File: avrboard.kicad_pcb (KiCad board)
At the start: 2 copper layers, 21 parts, among them IC1 ATMEGA328P-P, P1 FTDI, P2 ICSP, SW1 RESET, X1 16MHz

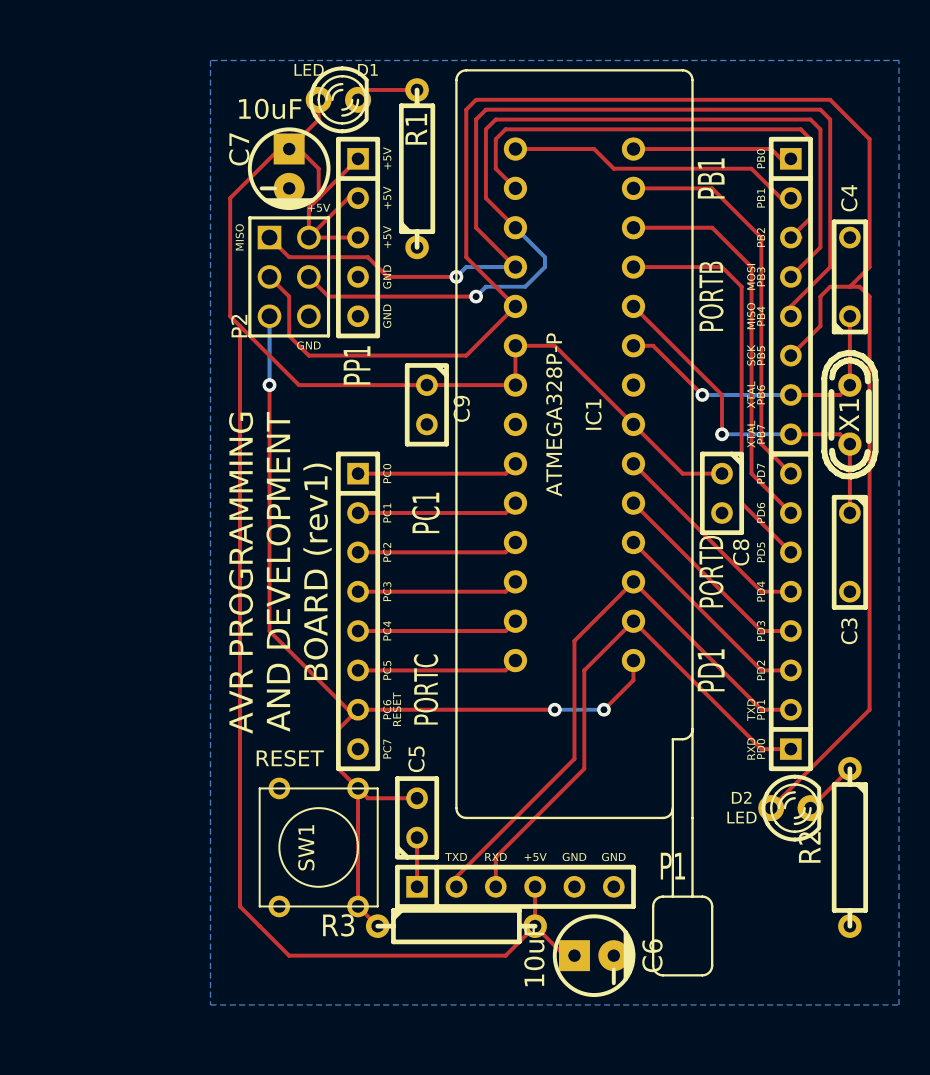
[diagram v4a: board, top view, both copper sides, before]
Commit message: Move the PORTB headers to the other side of the chip.
The routing is less crazy this way, since many of the port B pins are on
that side, and the power and port B headers can both fit together on that
side.
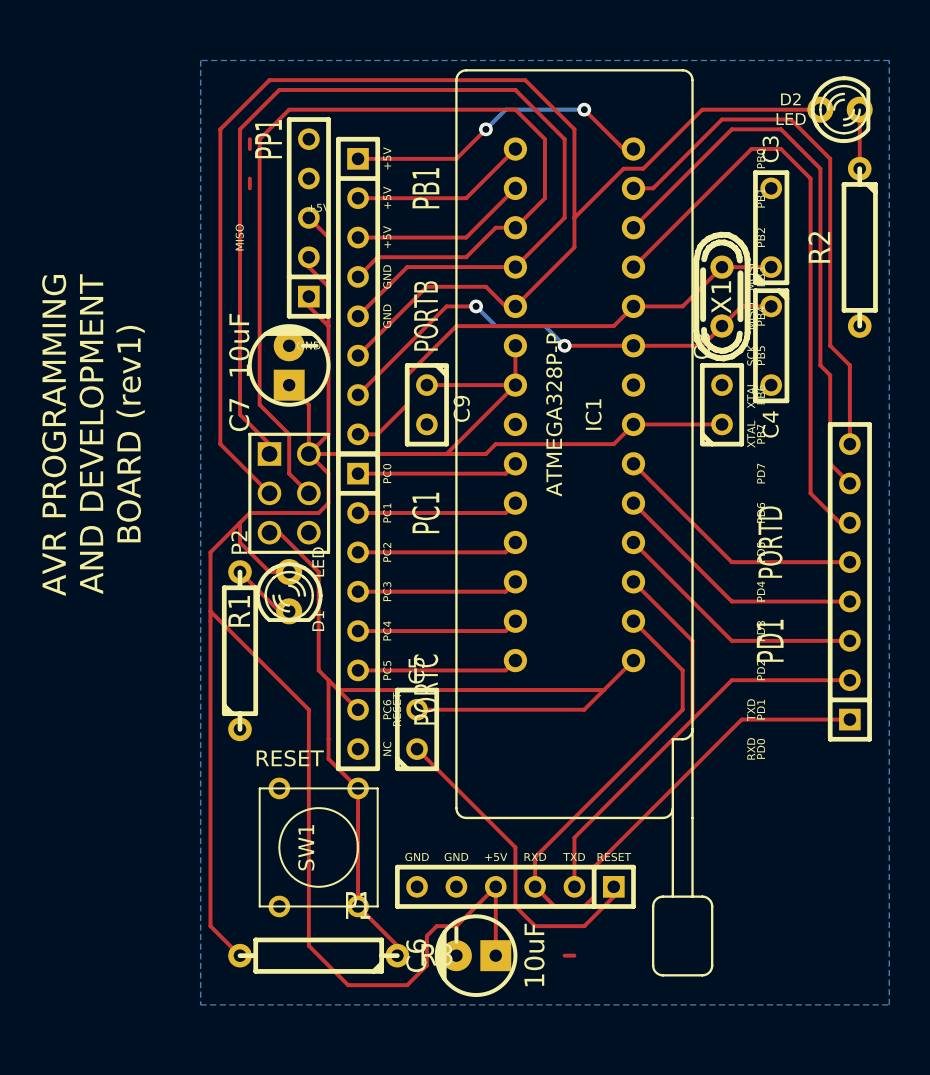
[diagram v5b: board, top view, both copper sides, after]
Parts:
- moved D2 45.2 mm to (164.5, 38.7)
- moved R2 38.7 mm to (165.7, 47.6)
- moved R1 33.1 mm to (125.7, 73.7)
- moved D1 31.9 mm to (128.9, 69.8), turned to 270 degrees
- moved PB1 27.9 mm to (133.3, 50.8)
- moved C3 21.6 mm to (160.0, 46.4), turned to 90 degrees
- moved P2 14.0 mm to (128.9, 63.5)
- moved C7 12.7 mm to (128.9, 55.2), turned to 0 degrees
- moved X1 11.2 mm to (156.8, 50.8), turned to 270 degrees
- moved R3 9.09 mm to (130.8, 93.3), turned to 180 degrees
- moved C6 7.62 mm to (141.0, 93.3), turned to 90 degrees
- moved C4 6.75 mm to (160.0, 54.0), turned to 270 degrees
- moved C5 5.72 mm to (137.2, 78.7)
- moved C8 5.72 mm to (156.8, 57.8), turned to 90 degrees
- moved PP1 4.96 mm to (130.2, 44.5), turned to 90 degrees
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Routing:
- net /PB5: track 116.1 -> 94.6 mm
- net /PB2: track 32.1 -> 11.5 mm
- net /+5V: track 139.5 -> 159.0 mm
- net Net-(C5-Pad1): track 3.18 -> 21.1 mm
- net /RXD: track 34.4 -> 49.4 mm
- net /PD5: track 26.0 -> 39.0 mm
- net /PD6: track 25.6 -> 36.9 mm
- net /PB6: track 20.0 -> 31.1 mm, vias 1 -> 2
- net /PB0: track 10.4 -> 20.1 mm, vias 0 -> 2
- net /PD7: track 25.6 -> 34.5 mm
- net /PB7: track 23.6 -> 32.3 mm, vias 1 -> 0
- net /PB1: track 19.1 -> 11.5 mm
- net /PD4: track 13.6 -> 16.6 mm
- net /PD3: track 13.6 -> 16.6 mm
- net /PD2: track 13.6 -> 16.6 mm
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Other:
- board text added: "NC"
- board text removed: "PC7"

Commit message: Clean up the silkscreen and remove some "bays" from the ground plane.
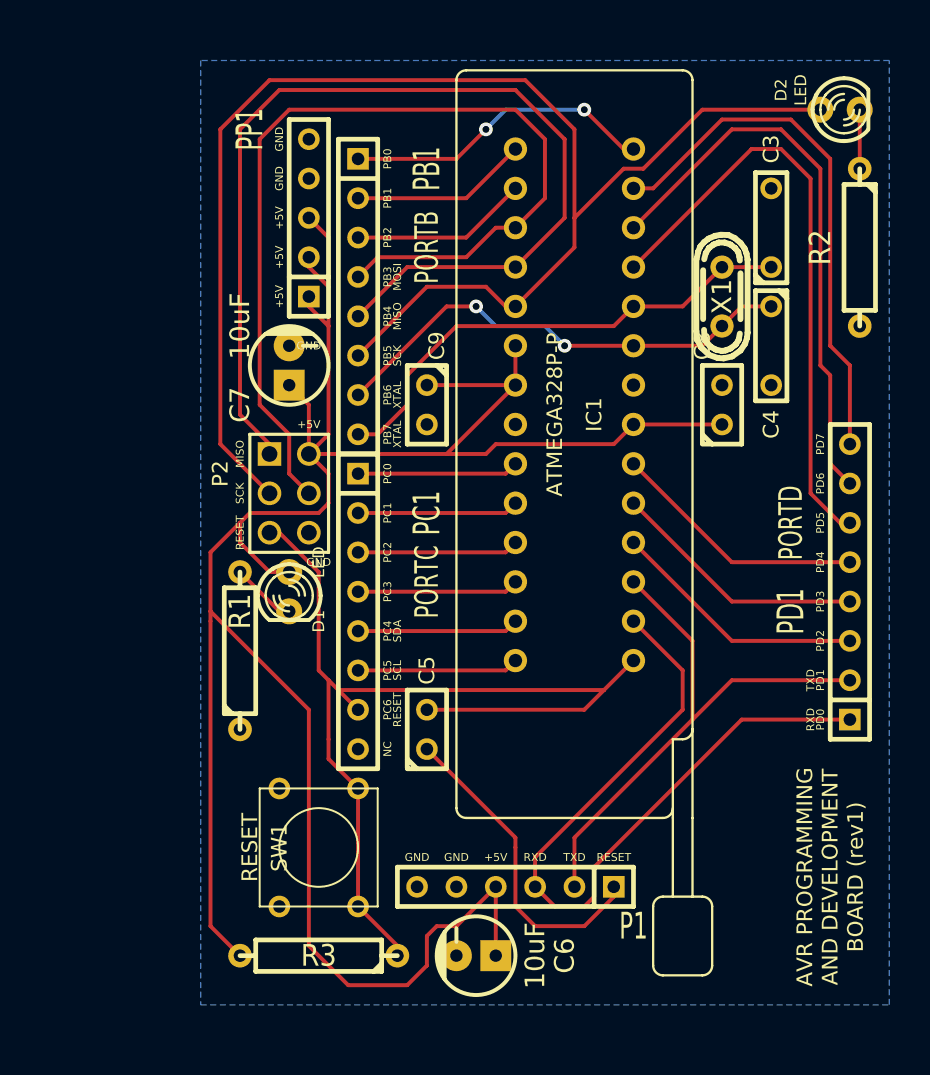
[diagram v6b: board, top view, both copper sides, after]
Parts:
- moved C5 0.63 mm to (137.8, 78.7)
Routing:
- net (no net): track 1.90 -> 0.00 mm
- net /RESET: track 66.2 -> 65.6 mm
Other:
- board text added: "SCL"
- board text added: "SDA"

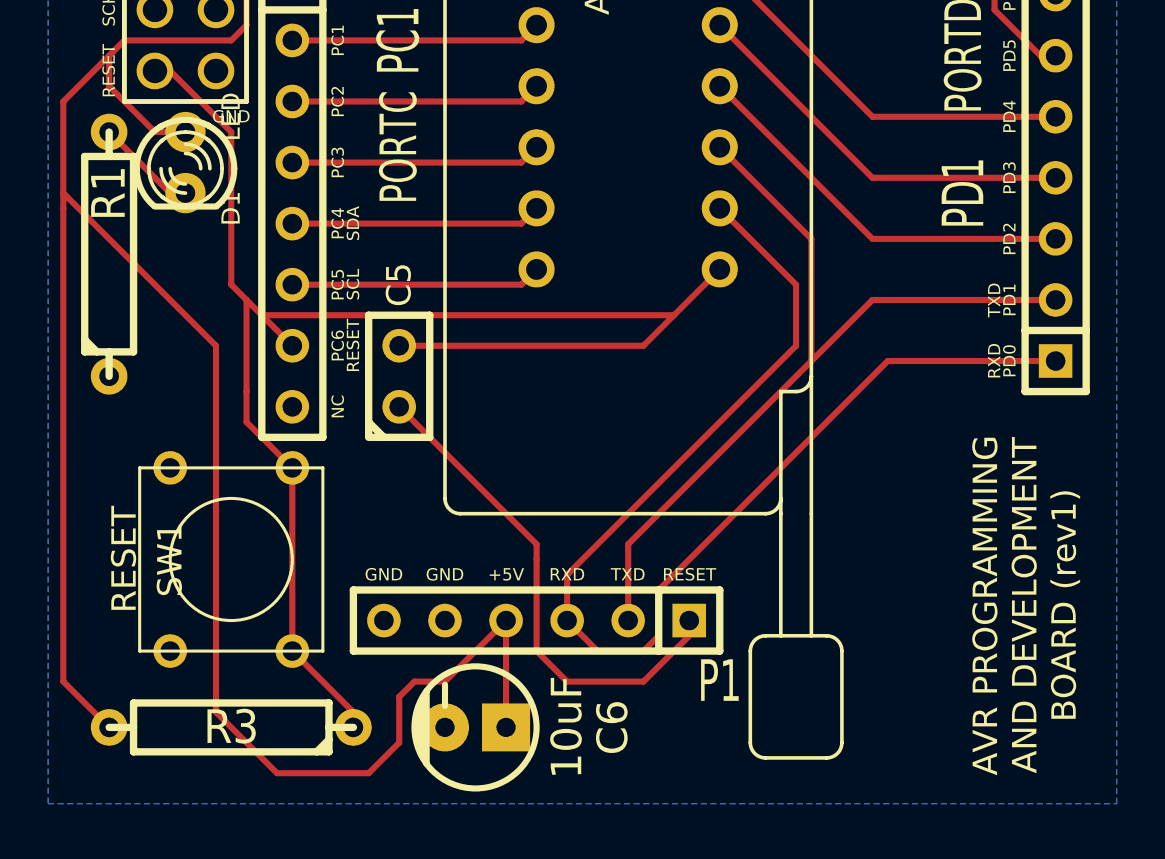
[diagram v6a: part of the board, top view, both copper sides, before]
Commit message: Move the FTDI socket over to increase clearance from the ZIF lever.
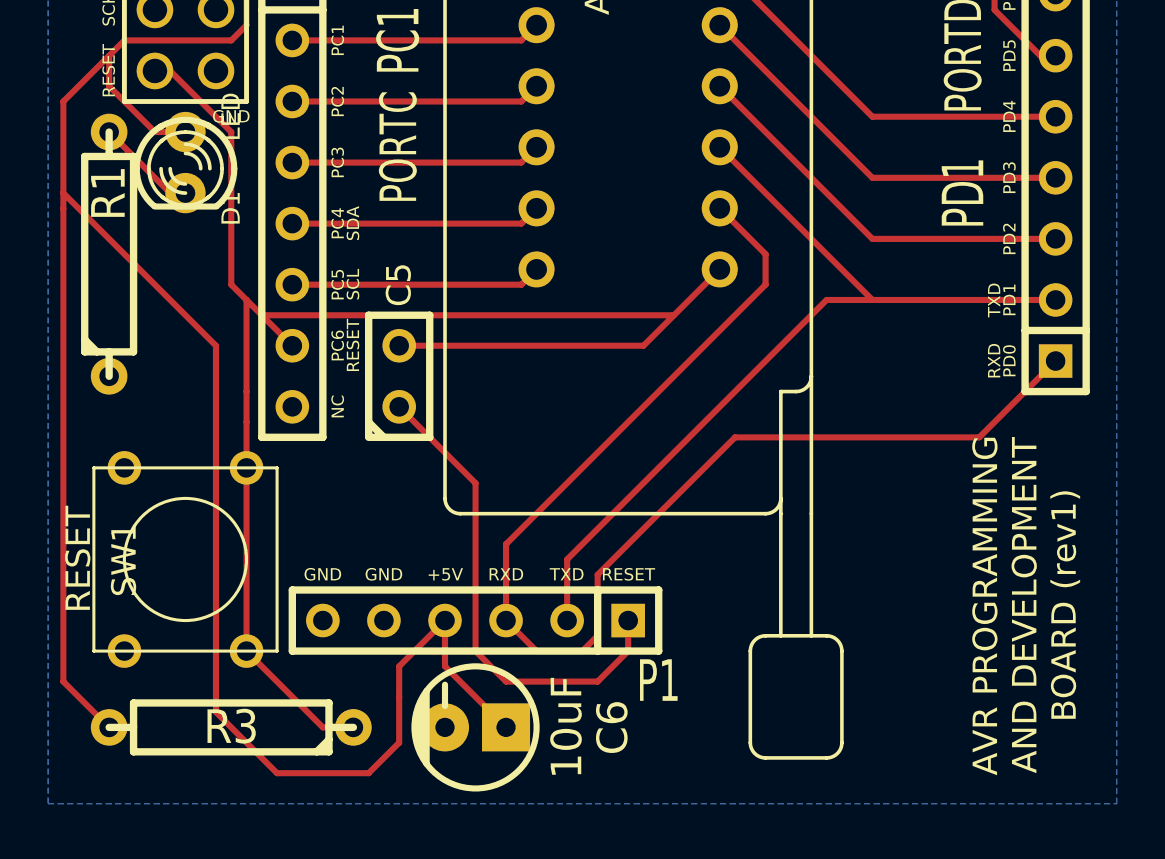
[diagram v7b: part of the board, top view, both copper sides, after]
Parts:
- moved P1 2.54 mm to (141.0, 88.9)
- moved SW1 1.91 mm to (128.9, 86.4)
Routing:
- net /RXD: track 49.4 -> 52.3 mm
- net /RESET: track 65.6 -> 66.3 mm
- net /+5V: track 159.0 -> 158.2 mm
- net Net-(C5-Pad1): track 20.8 -> 20.1 mm
- net /TXD: track 35.6 -> 36.3 mm

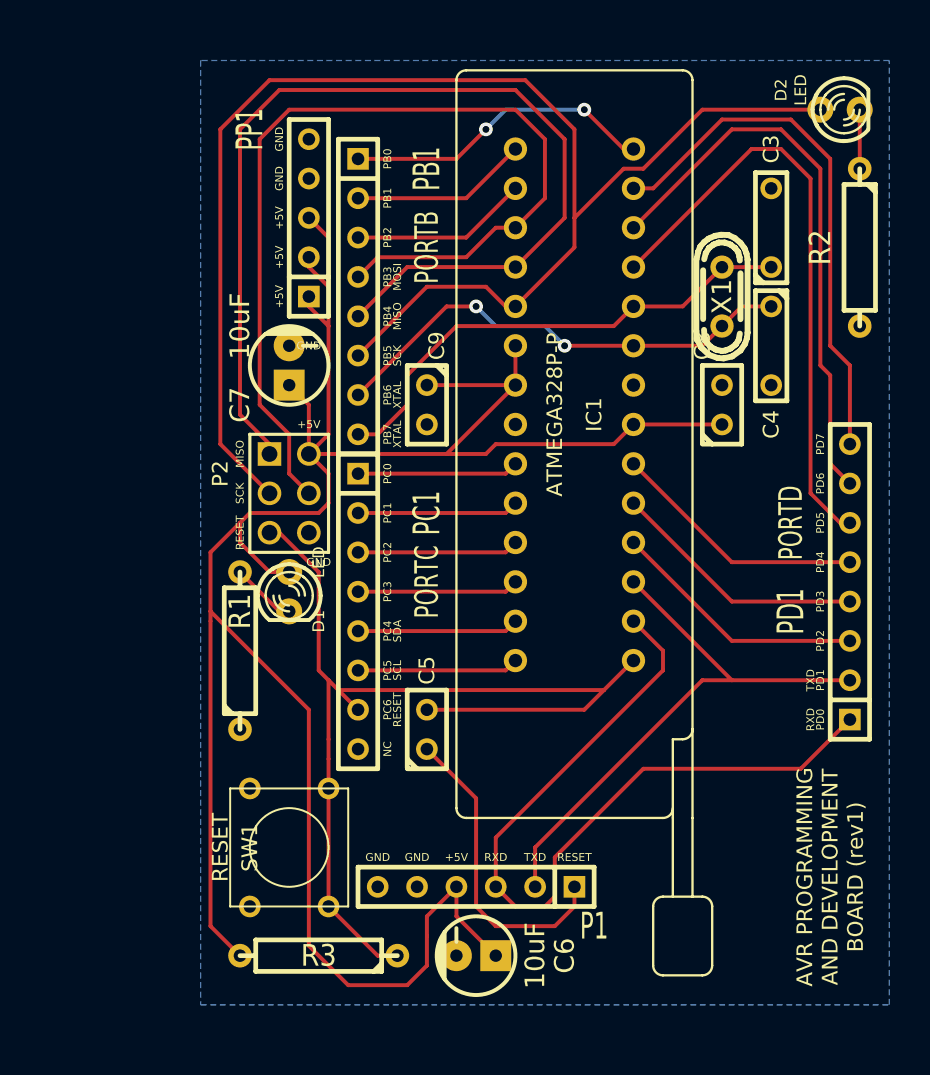
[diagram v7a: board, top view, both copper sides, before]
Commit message: Add board outline.
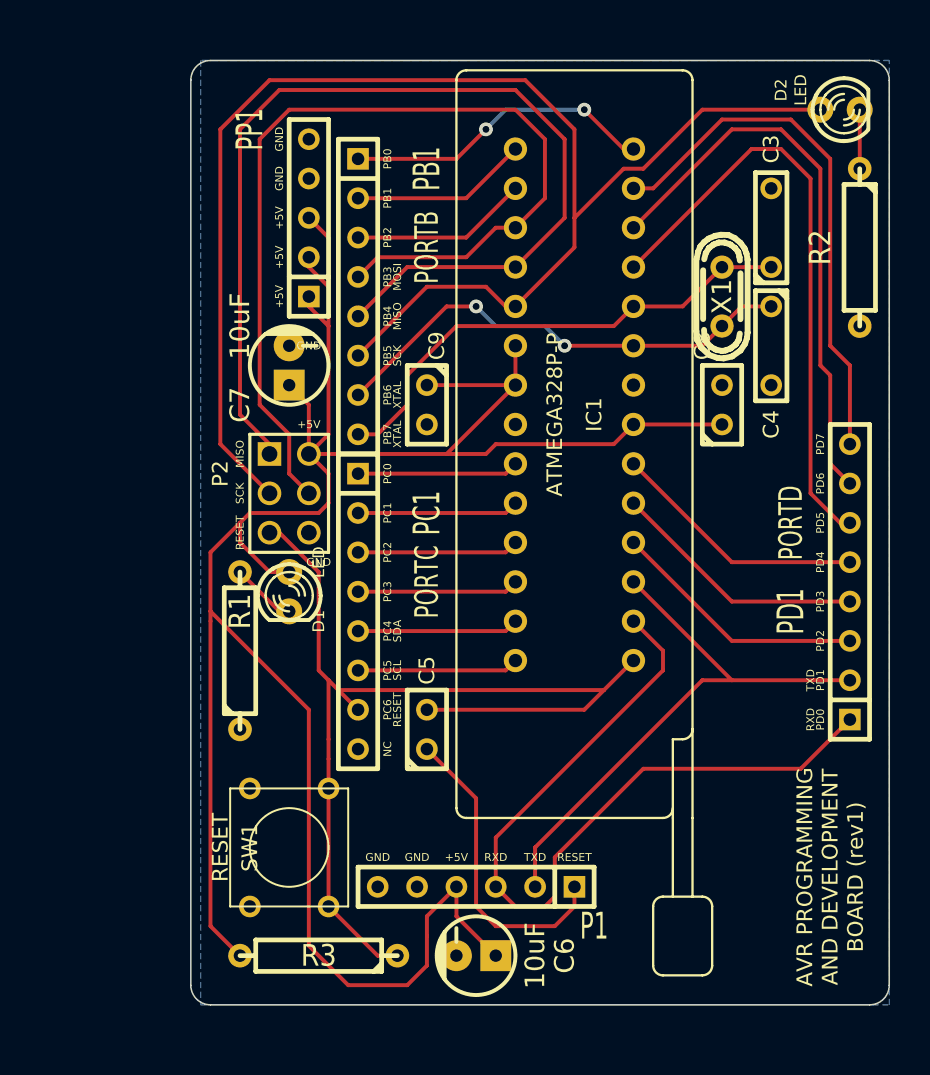
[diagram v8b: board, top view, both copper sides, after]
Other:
- board outline added: 45.1 x 61 mm
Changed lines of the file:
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@@
     (area 121.806305 35.56 167.904886 96.5835)
     (thickness 1.6)
-    (drawings 52)
+    (drawings 60)
     (tracks 200)
     (zones 0)
@@
     )
   )
+  (gr_line (start 166.37 96.52) (end 123.825 96.52) (angle 90) (layer Edge.Cuts) (width 0.1))
+  (gr_line (start 167.64 36.83) (end 167.64 95.25) (angle 90) (layer Edge.Cuts) (width 0.1))
+  (gr_line (start 123.825 35.56) (end 166.37 35.56) (angle 90) (layer Edge.Cuts) (width 0.1))
+  (gr_line (start 122.555 95.25) (end 122.555 36.83) (angle 90) (layer Edge.Cuts) (width 0.1))
+  (gr_arc (start 123.825 36.83) (end 122.555 36.83) (angle 90) (layer Edge.Cuts) (width 0.1))
+  (gr_arc (start 166.37 36.83) (end 166.37 35.56) (angle 90) (layer Edge.Cuts) (width 0.1))
+  (gr_arc (start 166.37 95.25) (end 167.64 95.25) (angle 90) (layer Edge.Cuts) (width 0.1))
+  (gr_arc (start 123.825 95.25) (end 123.825 96.52) (angle 90) (layer Edge.Cuts) (width 0.1))
   (gr_text RESET (at 125.73 66.04 90) (layer F.SilkS)
     (effects (font (size 0.5094 0.5094) (thickness 0.1137)))
